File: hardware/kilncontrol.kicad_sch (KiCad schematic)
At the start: 116 parts, among them J1 5V DC IN, J10 CT 30A/1V (opt), J11 UART / EXPANSION, J2 USB-C, J3 TC1 KILN (K), J4 TC2 CASE (K), J5 OLED 128x64 I2C, J6 SSR1 CTRL, J7 SSR2 CTRL (opt), J8 CONTACTOR COIL 5V, J9 BUZZER / AUX, Q1 AO3400A, Q2 AO3400A, Q3 AO3400A, Q4 AO3400A, SW1 RESET, SW2 BOOT, SW3 ENCODER, U1 ESP32-S3-WROOM-1, U2 AMS1117-3.3, U3 MAX31856, U4 MAX31856

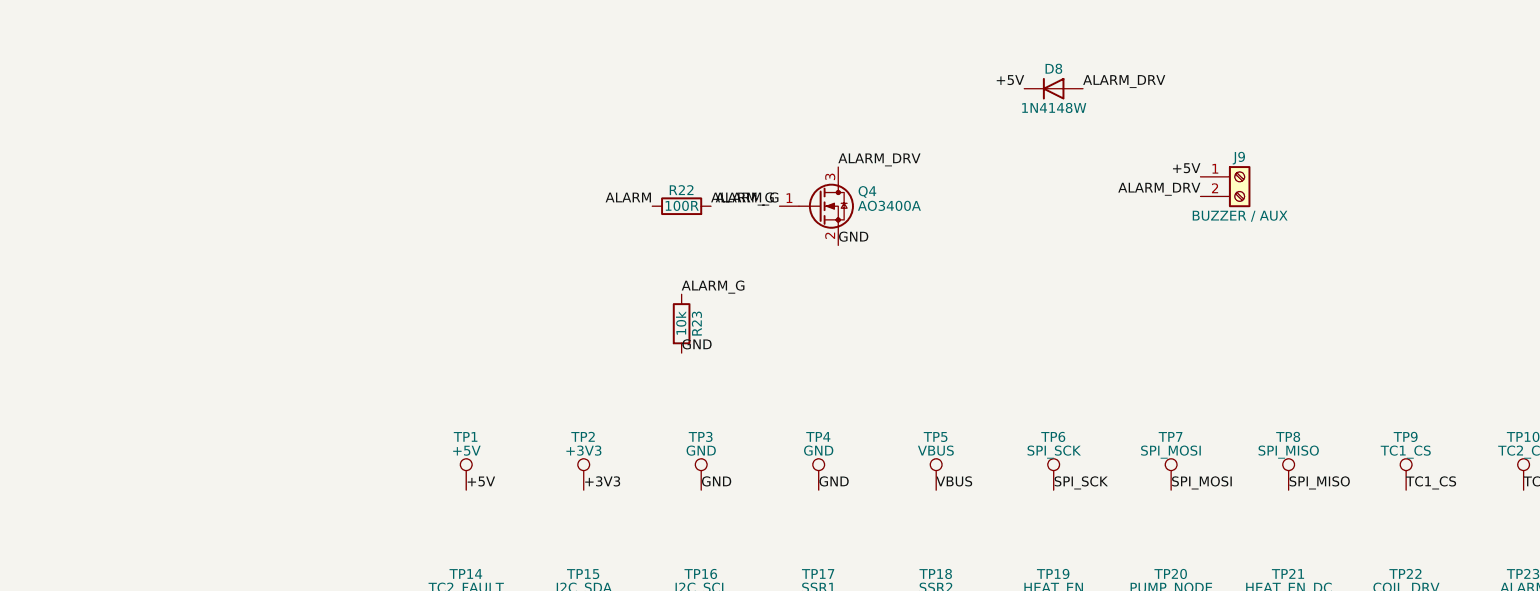
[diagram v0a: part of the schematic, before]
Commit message: Replace the external buzzer with an on-board one, shrink the test points
Buzzer
  J9, the screw terminal for an external buzzer, is replaced by BZ1 on the
  board: a TMB12A05, 5 V active (self-driving) magnetic buzzer, LCSC C96093.

  Active rather than passive: the 5 V-capable SMD passive part found on LCSC
  is rated 2.5-4.5 V and would be overdriven on the 5 V rail, and an active
  buzzer drops straight into the existing Q4 low-side driver and its flyback
  diode. No circuit change and no firmware change, because SR-20 asks the
  fault and completion alarms to be distinguishable by pattern, not by pitch,
  which kiln_alarm_pattern_t already does.

  This removes the auxiliary-relay output the old terminal also provided. The
  ALARM signal remains available at TP23 if an external annunciator is wanted
  later.

Test points
  All 33 change from TestPoint_THTPad_D2.0mm_Drill1.0mm to
  TestPoint_Pad_1.5x1.5mm: smaller, and SMD, so they sit on the top copper
  layer by construction rather than by layout discipline. The whole board can
  be probed without turning it over, and 33 drilled holes leave the board.

  A note on the sheet tells whoever does the placement not to move any test
  point to the bottom layer.

Requirements
  HR-09 now specifies an on-board buzzer rather than an alarm output capable
  of driving one. SR-20 reworded to match. New HR-19 (test points on the top
  layer only) and HR-20 (small pads, no drilled hole).

Housing
  The lid gains a perforated sound port above BZ1. A buzzer sealed inside the
  box is heavily muffled and SR-20 depends on the operator hearing it; a ring
  of 1.6 mm holes lets the sound out without leaving an opening large enough
  to drop debris onto the board.

Board
  Footprints imported from the schematic in KiCad since the last commit, and
  that import deleted the four M3 mounting holes, which are restored here.

  The imported footprints are STALE: they still carry J9, lack BZ1, and use
  the old 2 mm through-hole test pad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
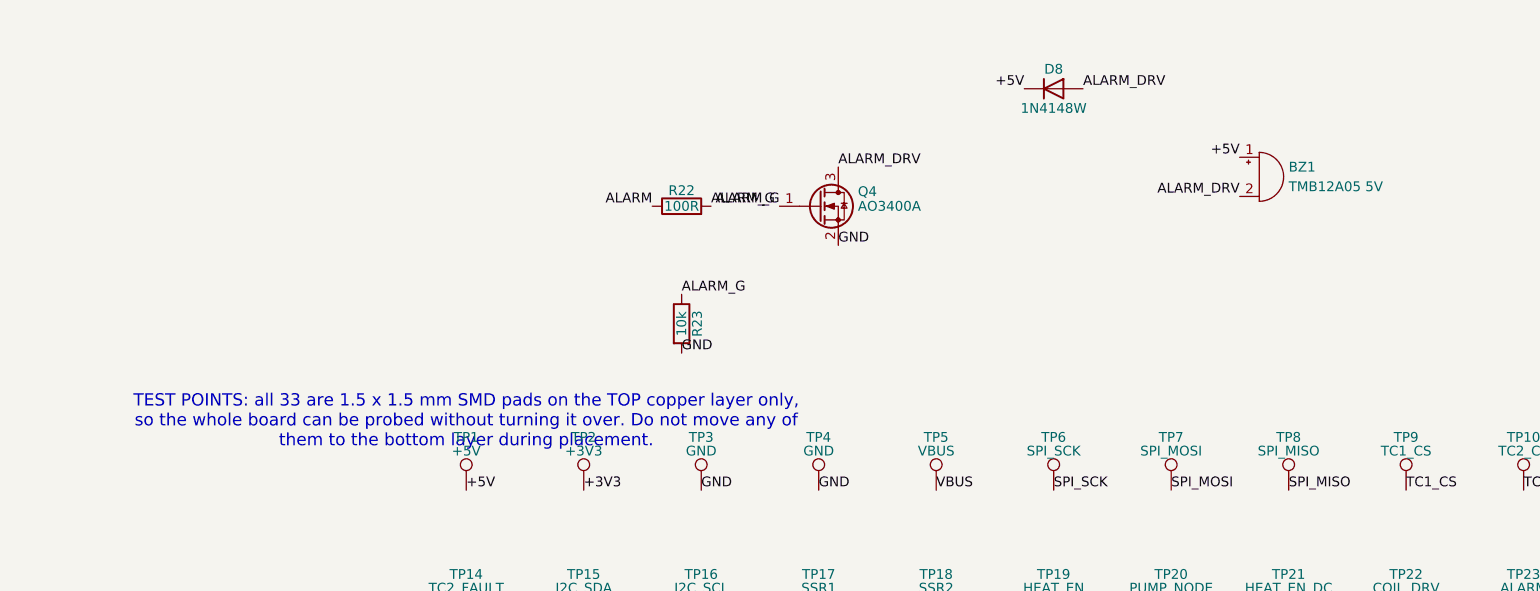
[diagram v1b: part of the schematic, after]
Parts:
- removed J9: BUZZER / AUX, TerminalBlock:TerminalBlock_MaiXu_MX126-5.0-02P_1x02_P5.00mm, symbol Connector:Screw_Terminal_01x02
- added BZ1: TMB12A05 5V, Buzzer_Beeper:Buzzer_12x9.5RM7.6, symbol Device:Buzzer
- TP1, TP10, TP11, TP12, TP13, TP14, TP15, TP16, TP17, TP18, TP19, TP2, TP20, TP21, TP22, TP23, TP24, TP25, TP26, TP27, TP28, TP29, TP3, TP30, TP31, TP32, TP33, TP4, TP5, TP6, TP7, TP8, TP9: footprint TestPoint:TestPoint_THTPad_D2.0mm_Drill1.0mm -> TestPoint:TestPoint_Pad_1.5x1.5mm
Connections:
- net +5V: now also BZ1.1 (+)
- net ALARM_DRV: now also BZ1.2 (-)
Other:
- note added: "TEST POINTS: all 33 are 1.5 x 1.5 mm SMD pads on the TOP copper layer only, so the whole board can be probed without turning it over. Do not move any of them to the bottom layer during placement."

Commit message: hw: interrupt the contactor coil from the fault pins and the lid
The coil circuit becomes a series chain of four independent interrupts, three
of which need no firmware at all:

  +5V -[J9 lid, NC]- J8 [COIL] -COIL_DRV- Q3 -COIL_RTN1- Q6 -COIL_RTN2- Q5 - GND
                                       charge pump    TC1 FAULT    TC2 FAULT

Q5 and Q6 are AO3400A with 10k gate pull-ups (R28, R29) to +3V3. J9's lid
contacts move into the coil supply so they carry coil current directly rather
than only being sensed. LID_SENSE brings the node back to IO38 through an
R30/R31 10k/18k divider, 5 V to 3.21 V, so SR-31 can still see the door; IO38
because IO2, IO3, IO45 and IO46 are strapping pins and HR-08 rules them out.

Each FAULT output drives its own MOSFET rather than being wire-ANDed onto one
node. Wire-ANDing would have merged TC1_FAULT and TC2_FAULT into a single net
and cost the per-device test points; a MOSFET each keeps both names, both
probe points, and buys two independent interrupts for the price of one part.

The flyback diode was on the wrong side of the new contact. D6's cathode went
to raw +5V, which the lid now bypasses, so opening the lid would have left the
coil with no freewheel path and put the inductive kick across the switch
contacts. Moved to the LID_SWITCH node so the loop is across the coil itself.
HR-25 records it so it cannot be undone by accident.

What this interlock is not: the FAULT outputs are open-drain, so an unpowered
or absent front end leaves its transistor on and the path closed, and the
MAX31856 detects an open circuit only once its fault mask is configured. They
interrupt on faults the device actively reports. SR-04 in firmware remains the
cover for a dead or unconfigured front end. The lid contact carries no such
caveat, being a contact in the circuit.

ERC unchanged at one error, the known U3 SDO output-output false positive.
Every net confirmed by query rather than by eye.

This commit also carries PCB layout and project state that w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
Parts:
- added J9: LID SWITCH, TerminalBlock:TerminalBlock_MaiXu_MX126-5.0-02P_1x02_P5.00mm, symbol Connector:Screw_Terminal_01x02
- added Q5, Q6: AO3400A, symbol Transistor_FET:Q_NMOS_GSD
- added R27: 1k, Resistor_SMD:R_0402_1005Metric, symbol Device:R
- added R28, R29, R30: 10k, symbol Device:R
- added R31: 18k, symbol Device:R
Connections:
- net +3V3: now also R28.1, R29.1; no longer C11.1, C12.1, C13.1, C17.1, C18.1, C19.1, C3.1, C4.1, C5.1, C6.1, D9.2 (K), J11.2 (Pin_2), J5.2 (Pin_2), R10.1, R11.1, R12.1, R24.1, R3.1, R8.1, R9.1, U1.2 (3V3), U2.2 (VO), U3.5 (AVDD), U3.8 (DVDD), U4.5 (AVDD), U4.8 (DVDD)
- net +5V: now also J9.1 (Pin_1), R27.1, R27.2; no longer D6.1 (K), J8.1 (Pin_1)
- net GND: now also SW1.1, SW2.1, Q5.2 (S), R31.2; no longer Q3.2 (S), SW1.2, SW2.2
- net MCU_EN: now also SW1.2; no longer SW1.1
- net MCU_IO0: now also SW2.2; no longer SW2.1
- net TC1_FAULT: now also Q6.1 (G), R28.2
- net TC2_FAULT: now also Q5.1 (G), R29.2
- net LID_SENSE: now reaches U1.31 (IO38)
- net LID_SENSE: now also R30.2, R31.1
- net ALARM_G: no longer names the net of Q4.1 (G), R22.2, R23.1
- net COIL_LED_A: no longer names the net of D7.2 (A), R21.2
- net PUMP_DRV: no longer names the net of C23.1, R19.2
- net SSR1_G: no longer names the net of Q1.1 (G), R13.2, R14.1
- net SSR1_LED_A: no longer names the net of D3.2 (A), R15.2
- net SSR2_G: no longer names the net of Q2.1 (G), R16.2, R17.1
- net SSR2_LED_A: no longer names the net of D4.2 (A), R18.2
- new net +3.3V: C11.1, C12.1, C13.1, C17.1, C18.1, C19.1, C3.1, C4.1, C5.1, C6.1, D9.2 (K), J11.2 (Pin_2), J5.2 (Pin_2), R10.1, R11.1, R12.1, R24.1, R3.1, R8.1, R9.1, U1.2 (3V3), U2.2 (VO), U3.5 (AVDD), U3.8 (DVDD), U4.5 (AVDD), U4.8 (DVDD)
- new net COIL_RTN1: Q3.2 (S), Q6.3 (D)
- new net COIL_RTN2: Q5.3 (D), Q6.2 (S)
- new net LID_SWITCH: D6.1 (K), J8.1 (Pin_1), J9.2 (Pin_2), R30.1
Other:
- note added: "AUX"
- note added: "All are 1.5 x 1.5 mm SMD pads on the TOP copper layer only, so the whole board can be probed without turning it over. Do not move any of them to the bottom layer during placement."
- note added: "CONTROLLER"
- note added: "DISPLAY"
- note added: "HEATER"
- note added: "POWER"
- note added: "TEMPERATURE"
- note added: "TEST POINTS"
- note removed: "TEST POINTS: all 33 are 1.5 x 1.5 mm SMD pads on the TOP copper layer only, so the whole board can be probed without turning it over. Do not move any of them to the bottom layer during placement."
- moved on the sheet: BZ1, C1, C10, C11, C12, C13, C14, C15, C16, C17, C18, C19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

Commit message: hw: pull the PCB up to the schematic, and start placement
The board had not been updated since section K went into the schematic --
update_pcb_from_schematic had never been run against it, which the tasklist
has been recording as an open item. It is run now, so the interlock chain's
parts exist on the board: J9, Q5, Q6 and R28 to R31 arrive as footprints, and
D4, J7, Q2 and R16 to R18 leave with the symbols they belonged to. R27 goes
from the schematic as well.

Placement is started, not finished: 74 footprints are repositioned, and
nothing is routed. There are no tracks and no vias on the board at all, and
the sixteen zones are untouched, so this is the arrangement pass and the
copper comes after it.

Both files are also written out in KiCad's current s-expression format, which
is why the diffs are far larger than the edits. Almost none of that is
whitespace -- `git diff -w` barely shrinks it -- so it is a genuine
restructuring of the files by the editor rather than a reflow, and it is not
worth trying to separate from the real changes.
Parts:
- removed D4: SSR2, LED_SMD:LED_0603_1608Metric, symbol Device:LED
- removed J7: SSR2 CTRL (opt), TerminalBlock:TerminalBlock_MaiXu_MX126-5.0-02P_1x02_P5.00mm, symbol Connector:Screw_Terminal_01x02
- removed Q2: AO3400A, Package_TO_SOT_SMD:SOT-23, symbol Transistor_FET:Q_NMOS_GSD
- removed R16: 100R, Resistor_SMD:R_0402_1005Metric, symbol Device:R
- removed R17: 10k, Resistor_SMD:R_0402_1005Metric, symbol Device:R
- removed R18, R27: 1k, Resistor_SMD:R_0402_1005Metric, symbol Device:R
- Q5, Q6: footprint (none) -> Package_TO_SOT_SMD:SOT-23
- R28, R29, R30, R31: footprint (none) -> Resistor_SMD:R_0402_1005Metric
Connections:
- net +3.3V: now also R28.1, R29.1
- net +3V3: no longer R28.1, R29.1
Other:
- note added: "CURRENT SENSE"
- moved on the sheet: BZ1, C25, C7, D8, D9, J10, J5, J9, Q4, Q5, Q6, R14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

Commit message: hw: another pass over the placement
94 of the 117 footprints move. Nothing is added or removed, the schematic is
unchanged in substance (256 wires, 49 junctions, 123 labels before and after,
reordered by the editor on save), and the board is still unrouted: zero tracks,
zero vias, the sixteen zones untouched.

So this is the arrangement continuing, not the copper starting. A23 and K4
still hold.
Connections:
- net TC1_N: now also J3.1 (Pin_1); no longer J3.2 (Pin_2)
- net TC1_P: now also J3.2 (Pin_2); no longer J3.1 (Pin_1)
- net TC2_N: now also J4.1 (Pin_1); no longer J4.2 (Pin_2)
- net TC2_P: now also J4.2 (Pin_2); no longer J4.1 (Pin_1)
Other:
- moved on the sheet: J3, J4
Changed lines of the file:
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@@
 	(wire
 		(pts
-			(xy 271.78 106.68) (xy 283.21 106.68)
+			(xy 441.96 147.32) (xy 448.31 147.32)
 		)
 		(stroke
@@
 	(wire
 		(pts
-			(xy 425.45 248.92) (xy 425.45 257.81)
+			(xy 271.78 106.68) (xy 283.21 106.68)
 		)
 		(stroke
@@
 	(wire
 		(pts
-			(xy 444.5 69.85) (xy 452.12 69.85)
+			(xy 425.45 248.92) (xy 425.45 257.81)
 		)
 		(stroke
@@
 	(wire
 		(pts
-			(xy 441.96 147.32) (xy 448.31 147.32)
-		)
-		(stroke
-			(width 0)
-			(type default)
-		)
-	)
-	(wire
-		(pts
 			(xy 223.52 81.28) (xy 220.98 81.28)
 		)
@@
 	(wire
 		(pts
+			(xy 444.5 69.85) (xy 452.12 69.85)
+		)
+		(stroke
+			(width 0)
+			(type default)
+		)
+	)
+	(wire
+		(pts
 			(xy 478.79 69.85) (xy 488.95 69.85)
 		)
@@
 	(symbol
 		(lib_id "Connector:Screw_Terminal_01x02")
-		(at 436.88 147.32 0)
-		(mirror y)
+		(at 436.88 149.86 180)
 		(unit 1)
 		(body_style 1)
@@
 		(dnp no)
 		(property "Reference" "J4"
-			(at 436.88 144.78 0)
+			(at 436.88 152.4 0)
 			(show_name no)
 			(do_not_autoplace no)
@@
 		)
 		(property "Value" "TC2 CASE (K)"
-			(at 436.88 152.4 0)
+			(at 436.88 144.78 0)
 			(show_name no)
 			(do_not_autoplace no)
@@
 		)
 		(property "Footprint" "TerminalBlock:TerminalBlock_MaiXu_MX126-5.0-02P_1x02_P5.00mm"
-			(at 436.88 147.32 0)
+			(at 436.88 149.86 0)
 			(hide yes)
 			(show_name no)
@@
 		)
 		(property "Datasheet" ""
-			(at 436.88 147.32 0)
+			(at 436.88 149.86 0)
 			(hide yes)
 			(show_name no)
@@
 		)
 		(property "Description" ""
-			(at 436.88 147.32 0)
+			(at 436.88 149.86 0)
 			(show_name no)
 			(do_not_autoplace no)
@@
 		)
 		(property "LCSC" "C474881"
-			(at 436.88 147.32 0)
+			(at 436.88 149.86 0)
 			(hide yes)
 			(show_name no)
@@
 	(symbol
 		(lib_id "Connector:Screw_Terminal_01x02")
-		(at 439.42 69.85 0)
-		(mirror y)
+		(at 439.42 72.39 180)
 		(unit 1)
 		(body_style 1)
@@
 		(dnp no)
 		(property "Reference" "J3"
-			(at 439.42 67.31 0)
+			(at 439.42 74.93 0)
 			(show_name no)
 			(do_not_autoplace no)
@@
 		)
 		(property "Value" "TC1 KILN (K)"
-			(at 439.42 74.93 0)
+			(at 439.42 67.31 0)
 			(show_name no)
 			(do_not_autoplace no)
@@
 		)
 		(property "Footprint" "TerminalBlock:TerminalBlock_MaiXu_MX126-5.0-02P_1x02_P5.00mm"
-			(at 439.42 69.85 0)
+			(at 439.42 72.39 0)
 			(hide yes)
 			(show_name no)
@@
 		)
 		(property "Datasheet" ""
-			(at 439.42 69.85 0)
+			(at 439.42 72.39 0)
 			(hide yes)
 			(show_name no)
@@
 		)
 		(property "Description" ""
-			(at 439.42 69.85 0)
+			(at 439.42 72.39 0)
 			(show_name no)
 			(do_not_autoplace no)
@@
 		)
 		(property "LCSC" "C474881"
-			(at 439.42 69.85 0)
+			(at 439.42 72.39 0)
 			(hide yes)
 			(show_name no)
